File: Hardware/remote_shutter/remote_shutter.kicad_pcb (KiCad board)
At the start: 4 copper layers, 78 x 57 mm, 62 parts, among them J1 USB_C_Receptacle_USB2.0, J2 OLED, J3 AudioJack3, J4 Buzzer, J6 Switch, Q1 DMN2056U, Q2 DMN2056U, Q3 BC847BDW1, SW1 RotaryEncoder_Switch, U1 AZ1117-3.3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

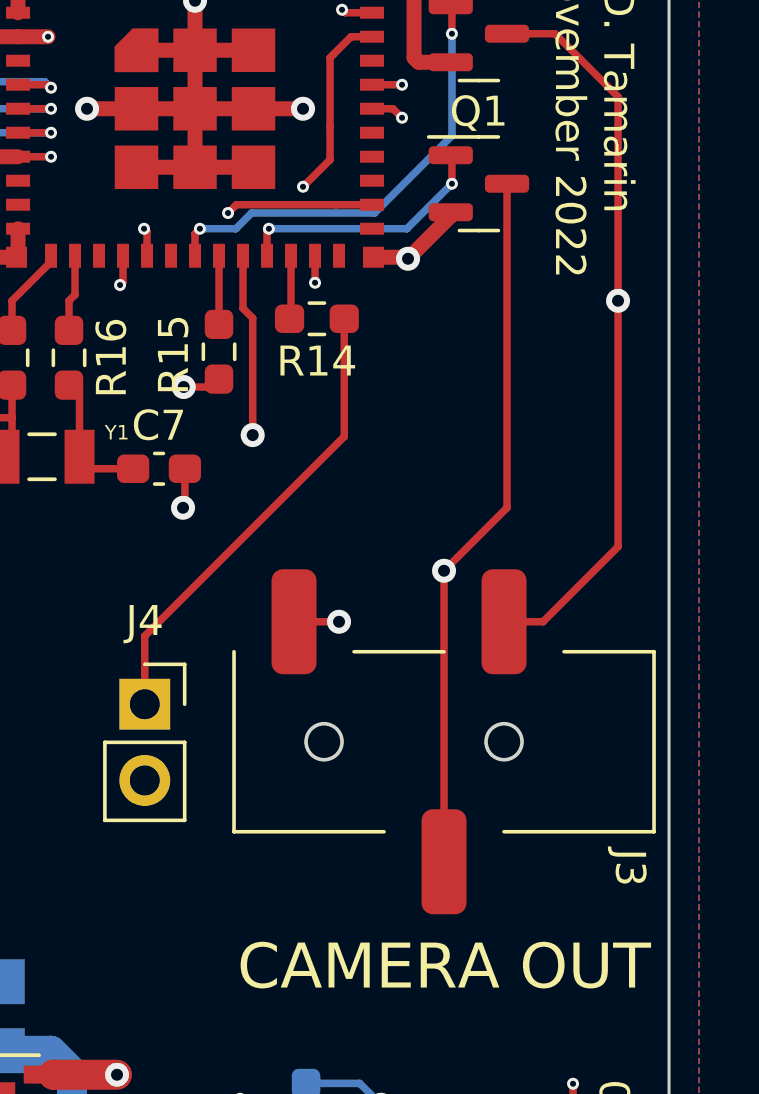
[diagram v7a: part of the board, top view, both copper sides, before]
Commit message: Fixed jack pinout
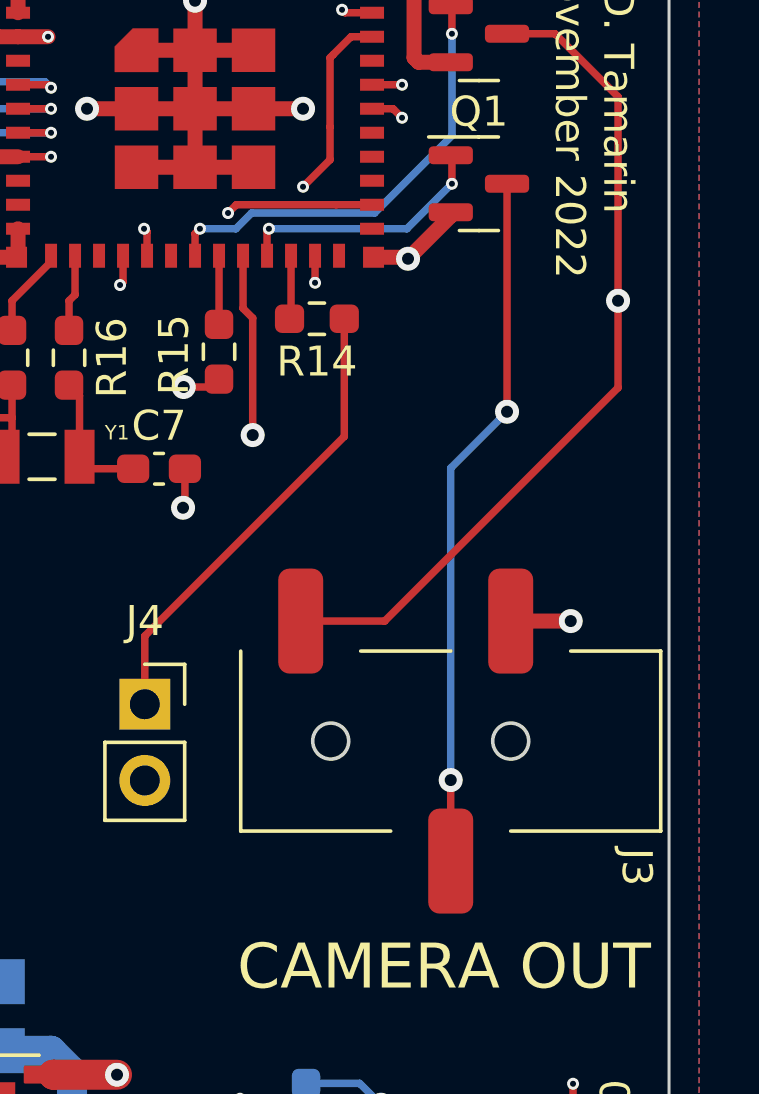
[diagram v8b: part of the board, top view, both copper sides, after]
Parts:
- moved J3 0.22 mm to (177.2, 96.5)
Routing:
- net /MCU/Interfaces/SHUTTER: track 87.1 -> 90.7 mm
- net GND: track 160.4 -> 160.9 mm
- net /MCU/Interfaces/FOCUS: track 80.4 -> 80.2 mm, vias 2 -> 3
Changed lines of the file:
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@@
   )
   (footprint "footprint:PJ-320B" (layer "F.Cu")
-    (at 176.9775 96.5225 -90)
+    (at 177.2 96.5 -90)
     (property "Sheetfile" "interfaces.kicad_sch")
     (property "Sheetname" "Interfaces")
@@
       (effects (font (size 1 1) (thickness 0.15)))
     )
-    (fp_line (start 3 0) (end 3 -5) (layer "F.SilkS") (width 0.12))
-    (fp_line (start 3 -5) (end -3 -5) (layer "F.SilkS") (width 0.12))
-    (fp_line (start -3 -5) (end -3 -2) (layer "F.SilkS") (width 0.12))
     (fp_line (start -3 9) (end 3 9) (layer "F.SilkS") (width 0.12))
-    (fp_line (start -3 2) (end -3 5) (layer "F.SilkS") (width 0.12))
     (fp_line (start 3 9) (end 3 4) (layer "F.SilkS") (width 0.12))
-    (fp_circle (center 0 6) (end 0.6 6) (layer "Edge.Cuts") (width 0.12) (fill none))
+    (fp_line (start 3 -5) (end -3 -5) (layer "F.SilkS") (width 0.12))
+    (fp_line (start -3 2) (end -3 5) (layer "F.SilkS") (width 0.12))
+    (fp_line (start 3 0) (end 3 -5) (layer "F.SilkS") (width 0.12))
+    (fp_line (start -3 -5) (end -3 -2) (layer "F.SilkS") (width 0.12))
     (fp_circle (center 0 0) (end 0.6 0) (layer "Edge.Cuts") (width 0.12) (fill none))
+    (fp_circle (center 0 6) (end 0.6 6) (layer "Edge.Cuts") (width 0.12) (fill none))
     (pad "R" smd roundrect (at 4 2 270) (size 3.5 1.5) (layers "F.Cu" "F.Paste" "F.Mask") (roundrect_rratio 0.25)
       (net 16 "/MCU/Interfaces/FOCUS") (pintype "passive"))
-    (pad "S" smd roundrect (at -4 7 270) (size 3.5 1.5) (layers "F.Cu" "F.Paste" "F.Mask") (roundrect_rratio 0.25)
+    (pad "S" smd roundrect (at -4 0 270) (size 3.5 1.5) (layers "F.Cu" "F.Paste" "F.Mask") (roundrect_rratio 0.25)
       (net 2 "GND") (pintype "passive"))
-    (pad "T" smd roundrect (at -4 0 270) (size 3.5 1.5) (layers "F.Cu" "F.Paste" "F.Mask") (roundrect_rratio 0.25)
+    (pad "T" smd roundrect (at -4 7 270) (size 3.5 1.5) (layers "F.Cu" "F.Paste" "F.Mask") (roundrect_rratio 0.25)
       (net 18 "/MCU/Interfaces/SHUTTER") (pintype "passive"))
   )
@@
   (segment (start 153.9775 112.5225) (end 153.5775 112.9225) (width 0.25) (layer "F.Cu") (net 2))
   (segment (start 160.7275 70.4725) (end 172.6275 70.4725) (width 0.5) (layer "F.Cu") (net 2))
+  (segment (start 179.2 92.5) (end 177.2 92.5) (width 0.5) (layer "F.Cu") (net 2))
   (segment (start 126.1275 72.4725) (end 127.1775 72.4725) (width 0.25) (layer "F.Cu") (net 2))
   (segment (start 168.6275 75.4225) (end 170.2775 75.4225) (width 0.5) (layer "F.Cu") (net 2))
@@
   (segment (start 113.4525 81.3725) (end 113.4525 81.9975) (width 0.25) (layer "F.Cu") (net 2))
   (segment (start 125.9725 80.9725) (end 125.9725 79.4275) (width 0.25) (layer "F.Cu") (net 2))
-  (segment (start 169.9775 92.5225) (end 171.4775 92.5225) (width 0.25) (layer "F.Cu") (net 2))
   (segment (start 153.94 113.285) (end 153.5775 112.9225) (width 1) (layer "F.Cu") (net 2))
   (segment (start 159.8275 80.3725) (end 159.7775 80.4225) (width 0.5) (layer "F.Cu") (net 2))
@@
   (via (at 166.3 84.698) (size 0.8) (drill 0.4) (layers "F.Cu" "B.Cu") (net 2))
   (via (at 113.4775 83.5225) (size 0.8) (drill 0.4) (layers "F.Cu" "B.Cu") (net 2))
-  (via (at 171.4775 92.5225) (size 0.8) (drill 0.4) (layers "F.Cu" "B.Cu") (net 2))
   (via (at 159.7775 80.4225) (size 0.8) (drill 0.4) (layers "F.Cu" "B.Cu") (net 2))
   (via (at 175.6775 110.8225) (size 0.8) (drill 0.4) (layers "F.Cu" "B.Cu") (net 2))
@@
   (via (at 137.8 86.6) (size 0.8) (drill 0.4) (layers "F.Cu" "B.Cu") (net 2))
   (via (at 153.5775 112.9225) (size 0.8) (drill 0.4) (layers "F.Cu" "B.Cu") (net 2))
+  (via (at 179.2 92.5) (size 0.8) (drill 0.4) (layers "F.Cu" "B.Cu") (net 2))
   (segment (start 173.09 122.235) (end 173.0775 122.2225) (width 0.25) (layer "B.Cu") (net 2))
   (segment (start 143.94 113.1225) (end 143.94 110.885) (width 0.25) (layer "B.Cu") (net 2))
@@
   (segment (start 169.14 79.4225) (end 173.74 79.4225) (width 0.25) (layer "B.Cu") (net 15))
   (segment (start 125.2275 85.4725) (end 130.665 85.4725) (width 0.25) (layer "F.Cu") (net 16))
-  (segment (start 177.0775 88.7225) (end 174.9775 90.8225) (width 0.25) (layer "F.Cu") (net 16))
+  (segment (start 177.0775 77.9225) (end 177.0775 85.5225) (width 0.25) (layer "F.Cu") (net 16))
   (segment (start 150.5275 85.4725) (end 134.5725 85.4725) (width 0.25) (layer "F.Cu") (net 16))
+  (segment (start 175.2 97.8) (end 175.2 100.5) (width 0.25) (layer "F.Cu") (net 16))
   (segment (start 134.5725 85.4725) (end 130.665 85.4725) (width 0.25) (layer "F.Cu") (net 16))
   (segment (start 134.6375 85.5375) (end 134.5725 85.4725) (width 0.25) (layer "F.Cu") (net 16))
   (segment (start 121.565 85.4725) (end 125.2275 85.4725) (width 0.25) (layer "F.Cu") (net 16))
   (segment (start 134.6375 86.7) (end 134.6375 85.5375) (width 0.25) (layer "F.Cu") (net 16))
-  (segment (start 174.9775 90.8225) (end 174.9775 100.5225) (width 0.25) (layer "F.Cu") (net 16))
-  (segment (start 177.0775 77.9225) (end 177.0775 88.7225) (width 0.25) (layer "F.Cu") (net 16))
   (segment (start 150.5775 85.4225) (end 150.5275 85.4725) (width 0.25) (layer "F.Cu") (net 16))
   (via (at 150.5775 85.4225) (size 0.8) (drill 0.4) (layers "F.Cu" "B.Cu") (net 16))
-  (via (at 174.9775 90.8225) (size 0.8) (drill 0.4) (layers "F.Cu" "B.Cu") (net 16))
-  (segment (start 150.5775 85.4225) (end 169.5775 85.4225) (width 0.25) (layer "In1.Cu") (net 16))
-  (segment (start 169.5775 85.4225) (end 174.9775 90.8225) (width 0.25) (layer "In1.Cu") (net 16))
+  (via (at 177.0775 85.5225) (size 0.8) (drill 0.4) (layers "F.Cu" "B.Cu") (net 16))
+  (via (at 175.2 97.8) (size 0.8) (drill 0.4) (layers "F.Cu" "B.Cu") (net 16))
+  (segment (start 176.9775 85.4225) (end 177.0775 85.5225) (width 0.25) (layer "In1.Cu") (net 16))
+  (segment (start 150.5775 85.4225) (end 176.9775 85.4225) (width 0.25) (layer "In1.Cu") (net 16))
+  (segment (start 175.2 87.4) (end 175.2 97.8) (width 0.25) (layer "B.Cu") (net 16))
+  (segment (start 177.0775 85.5225) (end 175.2 87.4) (width 0.25) (layer "B.Cu") (net 16))
   (segment (start 175.24 72.01) (end 175.2025 71.9725) (width 0.25) (layer "F.Cu") (net 17))
   (segment (start 175.24 72.9225) (end 175.24 72.01) (width 0.25) (layer "F.Cu") (net 17))
@@
   (segment (start 168.564511 78.897989) (end 172.664511 78.897989) (width 0.25) (layer "B.Cu") (net 17))
   (segment (start 134.4775 77.0225) (end 134.4275 76.9725) (width 0.25) (layer "F.Cu") (net 18))
-  (segment (start 176.9775 92.5225) (end 178.2775 92.5225) (width 0.25) (layer "F.Cu") (net 18))
   (segment (start 121.6775 76.9725) (end 125.4275 76.9725) (width 0.25) (layer "F.Cu") (net 18))
   (segment (start 134.6375 78.5) (end 134.6375 77.1825) (width 0.25) (layer "F.Cu") (net 18))
   (segment (start 178.6775 72.9225) (end 177.0775 72.9225) (width 0.25) (layer "F.Cu") (net 18))
   (segment (start 134.6375 77.1825) (end 134.4775 77.0225) (width 0.25) (layer "F.Cu") (net 18))
-  (segment (start 178.2775 92.5225) (end 180.7775 90.0225) (width 0.25) (layer "F.Cu") (net 18))
+  (segment (start 180.7775 81.8225) (end 180.7775 84.7225) (width 0.25) (layer "F.Cu") (net 18))
+  (segment (start 173 92.5) (end 170.2 92.5) (width 0.25) (layer "F.Cu") (net 18))
   (segment (start 125.4275 76.9725) (end 130.7775 76.9725) (width 0.25) (layer "F.Cu") (net 18))
   (segment (start 180.7775 81.8225) (end 180.7775 75.0225) (width 0.25) (layer "F.Cu") (net 18))
   (segment (start 180.7775 75.0225) (end 178.6775 72.9225) (width 0.25) (layer "F.Cu") (net 18))
-  (segment (start 180.7775 90.0225) (end 180.7775 81.8225) (width 0.25) (layer "F.Cu") (net 18))
+  (segment (start 180.7775 84.7225) (end 173 92.5) (width 0.25) (layer "F.Cu") (net 18))
   (segment (start 134.4275 76.9725) (end 130.7775 76.9725) (width 0.25) (layer "F.Cu") (net 18))
   (via (at 134.4775 77.0225) (size 0.8) (drill 0.4) (layers "F.Cu" "B.Cu") (net 18))
